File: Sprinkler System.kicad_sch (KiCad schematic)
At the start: 0 parts

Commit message: Ready to Send
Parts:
- added C1, C3: 10u, Capacitor_SMD:C_0805_2012Metric_Pad1.18x1.45mm_HandSolder, symbol Device:C_Small
- added C11, C12, C13, C14, C15, C16: 100n, Capacitor_SMD:C_0805_2012Metric_Pad1.18x1.45mm_HandSolder, symbol Device:C
- added C2: 22u, Capacitor_SMD:C_0805_2012Metric_Pad1.18x1.45mm_HandSolder, symbol Device:C_Small
- added F1: 1A, Sprinkler System:Fuseholder_5x20mm_15mm_Pins, symbol Device:Fuse
- added F2: 2A, Sprinkler System:Fuseholder_5x20mm_15mm_Pins, symbol Device:Fuse
- added J1: Main Supply, Connector_Phoenix_MC:PhoenixContact_MC_1,5_3-G-3.81_1x03_P3.81mm_Horizontal, symbol Connector:Screw_Terminal_01x03
- added J11: Station_0, Connector_Phoenix_MC:PhoenixContact_MC_1,5_2-G-3.81_1x02_P3.81mm_Horizontal, symbol Connector:Screw_Terminal_01x02
- added J12: Station_1, Connector_Phoenix_MC:PhoenixContact_MC_1,5_2-G-3.81_1x02_P3.81mm_Horizontal, symbol Connector:Screw_Terminal_01x02
- added J13: Station_2, Connector_Phoenix_MC:PhoenixContact_MC_1,5_2-G-3.81_1x02_P3.81mm_Horizontal, symbol Connector:Screw_Terminal_01x02
- added J14: Station_3, Connector_Phoenix_MC:PhoenixContact_MC_1,5_2-G-3.81_1x02_P3.81mm_Horizontal, symbol Connector:Screw_Terminal_01x02
- added J15: Station_4, Connector_Phoenix_MC:PhoenixContact_MC_1,5_2-G-3.81_1x02_P3.81mm_Horizontal, symbol Connector:Screw_Terminal_01x02
- added J16: Station_5, Connector_Phoenix_MC:PhoenixContact_MC_1,5_2-G-3.81_1x02_P3.81mm_Horizontal, symbol Connector:Screw_Terminal_01x02
- added J17: Conn_Button, Connector_JST:JST_XH_B6B-XH-A_1x06_P2.50mm_Vertical, symbol Connector_Generic:Conn_01x06
- added J2: XFMR, Connector_Phoenix_MC:PhoenixContact_MC_1,5_3-G-3.81_1x03_P3.81mm_Horizontal, symbol Connector:Screw_Terminal_01x03
- added J3: I2C, Connector_JST:JST_XH_B4B-XH-A_1x04_P2.50mm_Vertical, symbol Connector_Generic:Conn_01x04
- added J4: UART0, Connector_JST:JST_XH_B4B-XH-A_1x04_P2.50mm_Vertical, symbol Connector_Generic:Conn_01x04
- added K1: G3MB-202P, Sprinkler System:RELAY_G3MB-202P, symbol Sprinker System:G3MB-202P
- added K11, K12, K13, K14, K15, K16: G5LE-1, Relay_THT:Relay_SPDT_Omron-G5LE-1, symbol Relay:G5LE-1
- added LED1: IO2, LED_SMD:LED_0805_2012Metric_Pad1.15x1.40mm_HandSolder, symbol Device:LED_Small
- added LED2: PWR, LED_SMD:LED_0805_2012Metric_Pad1.15x1.40mm_HandSolder, symbol Device:LED_Small
- added R1, R3: 10k, Resistor_SMD:R_0805_2012Metric_Pad1.20x1.40mm_HandSolder, symbol Device:R
- added R11, R12, R13, R14, R15, R16: 100, Resistor_SMD:R_0805_2012Metric_Pad1.20x1.40mm_HandSolder, symbol Device:R
- added R2, R4: 470, Resistor_SMD:R_0805_2012Metric_Pad1.20x1.40mm_HandSolder, symbol Device:R
- added R32, R33, R34, R35: 10k, Resistor_SMD:R_0805_2012Metric_Pad1.20x1.40mm_HandSolder, symbol Device:R_Small
- added R5, R6: 4k7, Resistor_SMD:R_0805_2012Metric_Pad1.20x1.40mm_HandSolder, symbol Device:R_Small
- added RV11, RV12, RV13, RV14, RV15, RV16: 47V, Varistor:RV_Disc_D15.5mm_W5.4mm_P7.5mm, symbol Device:Varistor
- added SW1: EN, Button_Switch_SMD:SW_Push_SPST_NO_Alps_SKRK, symbol Switch:SW_Push
- added SW2: BOOT, Button_Switch_SMD:SW_Push_SPST_NO_Alps_SKRK, symbol Switch:SW_Push
- added U1: HLK-PM01, Converter_ACDC:Converter_ACDC_Hi-Link_HLK-PMxx, symbol Converter_ACDC:HLK-PM01
- added U2: ULN2803A, Package_SO:SOIC-18W_7.5x11.6mm_P1.27mm, symbol Transistor_Array:ULN2803A
- added U3: AMS1117-3.3, Package_TO_SOT_SMD:SOT-223-3_TabPin2, symbol Regulator_Linear:AMS1117-3.3
- added U4: ESP32-WROOM-32U, RF_Module:ESP32-WROOM-32U, symbol RF_Module:ESP32-WROOM-32U
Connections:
- new net: R2.1, SW1.2
- new net: C11.2, R11.1
- new net: R4.1, SW2.2
- new net: C12.2, R12.1
- new net: LED1.1 (K), R5.1
- new net: C13.2, R13.1
- new net: C14.2, R14.1
- new net: C16.2, R16.1
- new net: LED2.1 (K), R6.1
- new net: C15.2, R15.1
- new net +3V3: C2.1, C3.1, J17.2 (Pin_2), LED2.2 (A), R1.1, R3.1, U3.2 (VO), U4.2 (VDD)
- new net +5V: C1.1, J3.2 (Pin_2), J4.2 (Pin_2), K1.3, K11.5, K12.5, K13.5, K14.5, K15.5, K16.5, U1.4 (+Vout), U2.10 (COM), U3.3 (VI)
- new net 24VAC: C11.1, C12.1, C13.1, C14.1, C15.1, C16.1, F2.2, K11.1, K12.1, K13.1, K14.1, K15.1, K16.1, RV11.1, RV12.1, RV13.1, RV14.1, RV15.1, RV16.1
- new net 24VAC_Supply: F2.1, J2.3 (Pin_3)
- new net 24V_On: U2.8 (I8), U4.27 (IO16)
- new net 24V_S0: J11.2 (Pin_2), K11.3, R11.2, RV11.2
- new net 24V_S1: J12.2 (Pin_2), K12.3, R12.2, RV12.2
- new net 24V_S2: J13.2 (Pin_2), K13.3, R13.2, RV13.2
- new net 24V_S3: J14.2 (Pin_2), K14.3, R14.2, RV14.2
- new net 24V_S4: J15.2 (Pin_2), K15.3, R15.2, RV15.2
- new net 24V_S5: J16.2 (Pin_2), K16.3, R16.2, RV16.2
- new net Coil0: K11.2, U2.12 (O7)
- new net Coil1: K12.2, U2.13 (O6)
- new net Coil2: K13.2, U2.14 (O5)
- new net Coil3: K14.2, U2.15 (O4)
- new net Coil4: K15.2, U2.16 (O3)
- new net Coil5: K16.2, U2.17 (O2)
- new net EN: R1.2, SW1.1, U4.3 (EN)
- new net GND: C1.2, C2.2, C3.2, J1.1 (Pin_1), J17.1 (Pin_1), J3.1 (Pin_1), J4.1 (Pin_1), R2.2, R32.2, R33.2, R34.2, R35.2, R4.2, R5.2, R6.2, U1.3 (-Vout), U2.9 (GND), U3.1 (GND), U4.1 (GND), U4.15 (GND), U4.38 (GND), U4.39 (GND)
- new net IO0: R3.2, SW2.1, U4.25 (IO0)
- new net IO1: J4.4 (Pin_4), U4.35 (TXD0/IO1)
- new net IO2: LED1.2 (A), U4.24 (IO2)
- new net IO3: J4.3 (Pin_3), U4.34 (RXD0/IO3)
- new net IO32: J17.5 (Pin_5), R32.1, U4.8 (IO32)
- new net IO33: J17.6 (Pin_6), R33.1, U4.9 (IO33)
- new net IO34: J17.3 (Pin_3), R34.1, U4.6 (IO34)
- new net IO35: J17.4 (Pin_4), R35.1, U4.7 (IO35)
- new net L: F1.2, K1.1, U1.1 (AC/L)
- new net L_SW: J2.1 (Pin_1), K1.2
- new net L_Supply: F1.1, J1.2 (Pin_2)
- new net Neut: J1.3 (Pin_3), J11.1 (Pin_1), J12.1 (Pin_1), J13.1 (Pin_1), J14.1 (Pin_1), J15.1 (Pin_1), J16.1 (Pin_1), J2.2 (Pin_2), U1.2 (AC/N)
- new net SCL: J3.4 (Pin_4), U4.26 (IO4)
- new net SDA: J3.3 (Pin_3), U4.29 (IO5)
- new net SSR: K1.4, U2.11 (O8)
- new net Zone0: U2.7 (I7), U4.28 (IO17)
- new net Zone1: U2.6 (I6), U4.30 (IO18)
- new net Zone2: U2.5 (I5), U4.31 (IO19)
- new net Zone3: U2.4 (I4), U4.33 (IO21)
- new net Zone4: U2.3 (I3), U4.36 (IO22)
- new net Zone5: U2.2 (I2), U4.37 (IO23)
- no-connect marks 0 -> 23

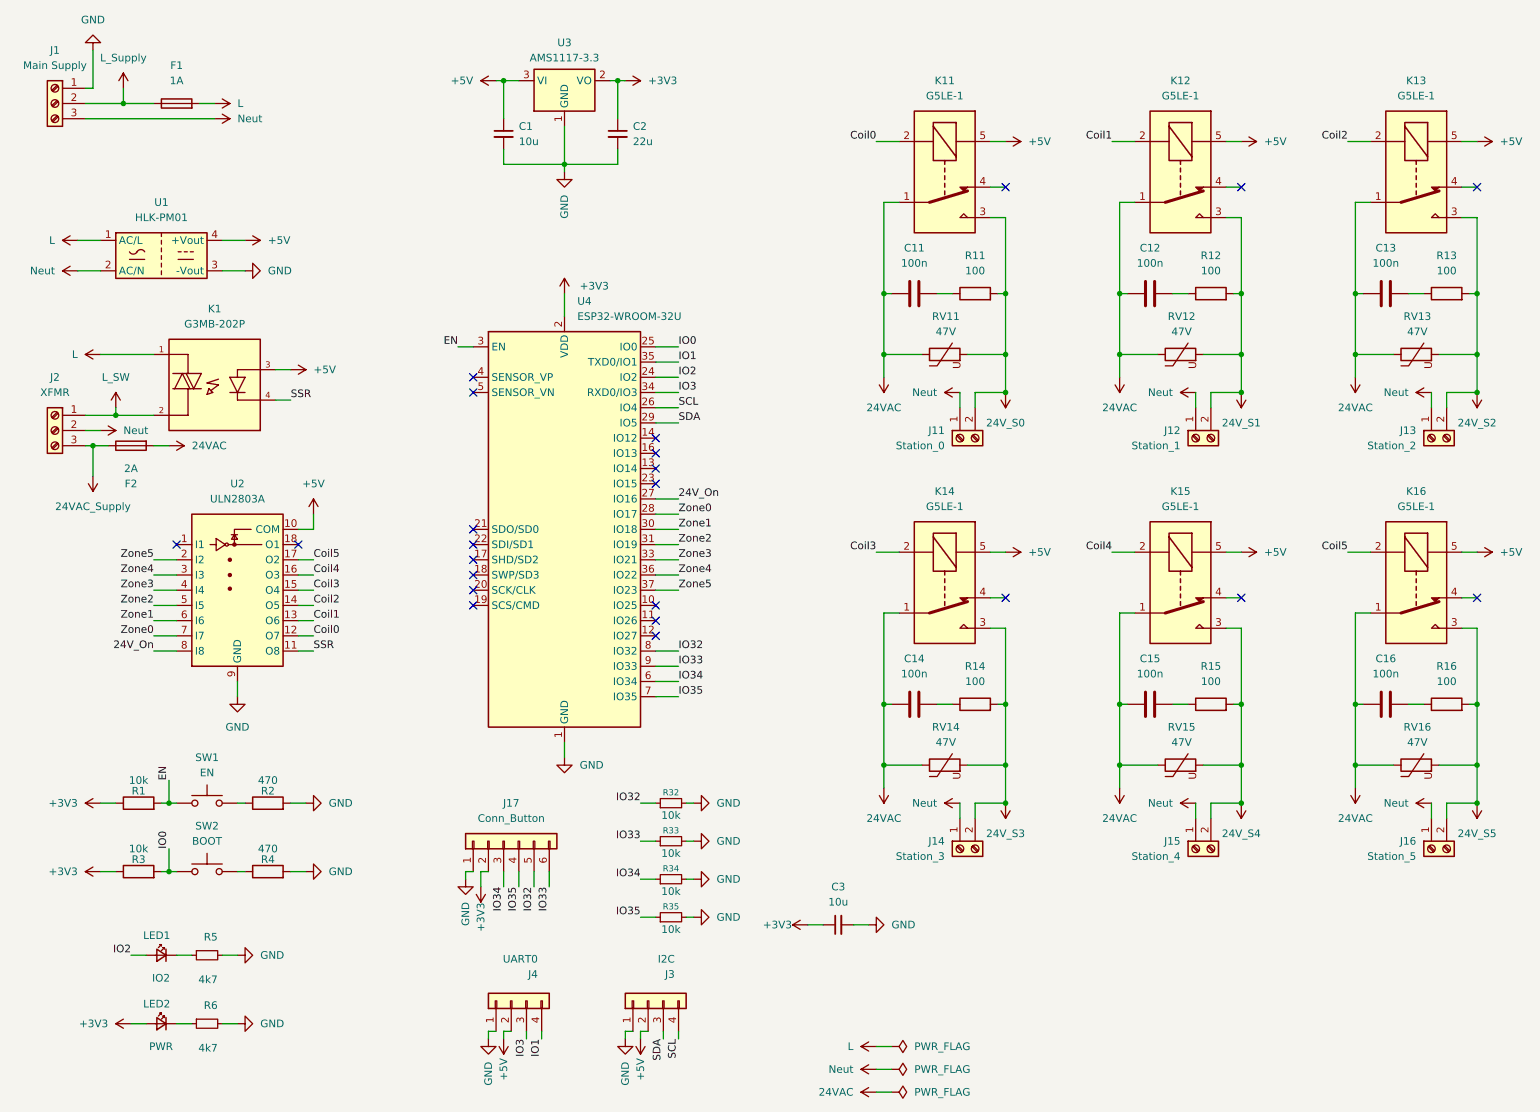
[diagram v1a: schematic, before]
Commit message: feat: advance 6-zone sprinkler controller design and documentation
* replace template docs with full project README (safety notes, enclosure guidance, power/control paths, wiring, BOM, GPIO map)
* update schematic and PCB with major reannotation/layout changes, added test points, and 24 VAC net handling refinements
* add/update project rule settings (new 24VAC net class, net class priorities, DRC exclusion updates)
* adjust relay footprint 3D model orientation/offset
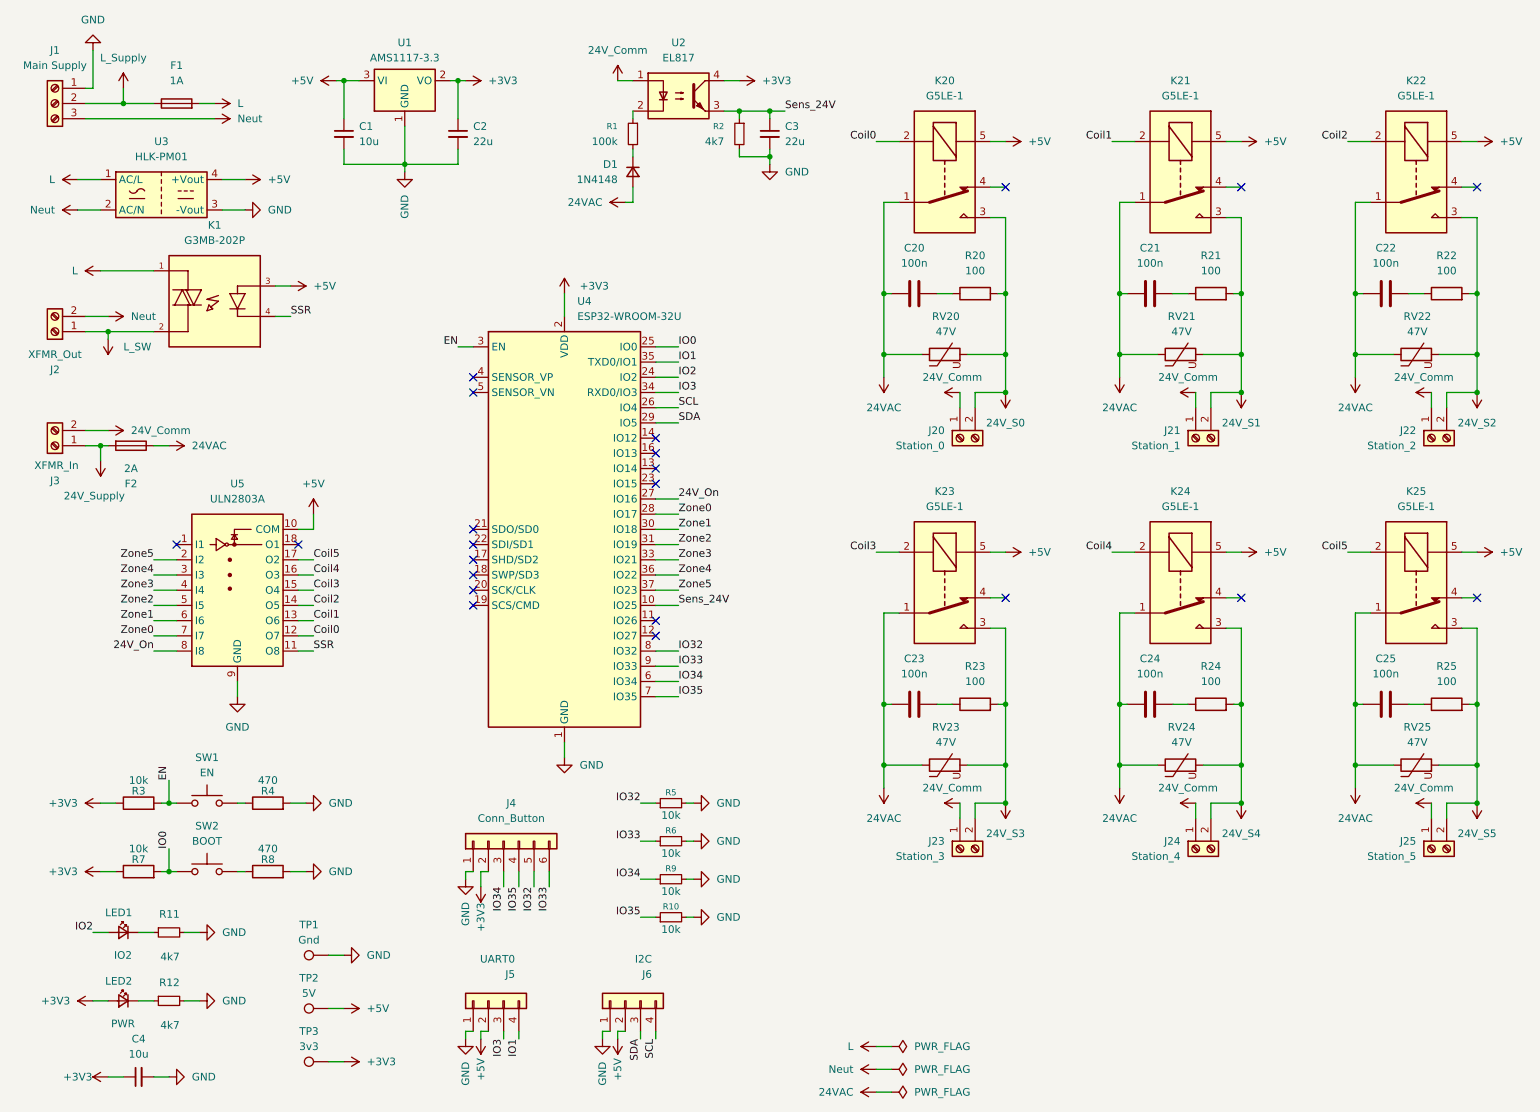
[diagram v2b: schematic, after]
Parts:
- removed J2: XFMR, Connector_Phoenix_MC:PhoenixContact_MC_1,5_3-G-3.81_1x03_P3.81mm_Horizontal, symbol Connector:Screw_Terminal_01x03
- added C3: 22u, Capacitor_SMD:C_0805_2012Metric_Pad1.18x1.45mm_HandSolder, symbol Device:C_Small
- added D1: 1N4148, Diode_SMD:D_0805_2012Metric_Pad1.15x1.40mm_HandSolder, symbol Device:D_Small
- added J2: XFMR_Out, TerminalBlock_Phoenix:TerminalBlock_Phoenix_PT-1,5-2-5.0-H_1x02_P5.00mm_Horizontal, symbol Connector:Screw_Terminal_01x02
- added J3: XFMR_In, TerminalBlock_Phoenix:TerminalBlock_Phoenix_PT-1,5-2-5.0-H_1x02_P5.00mm_Horizontal, symbol Connector:Screw_Terminal_01x02
- added R1: 100k, Resistor_SMD:R_0805_2012Metric_Pad1.20x1.40mm_HandSolder, symbol Device:R_Small
- added R2: 4k7, Resistor_SMD:R_0805_2012Metric_Pad1.20x1.40mm_HandSolder, symbol Device:R_Small
- added TP1: Gnd, TestPoint:TestPoint_Pad_D1.5mm, symbol Connector:TestPoint
- added TP2: 5V, TestPoint:TestPoint_Pad_D1.5mm, symbol Connector:TestPoint
- added TP3: 3v3, TestPoint:TestPoint_Pad_D1.5mm, symbol Connector:TestPoint
- added U2: EL817, Package_SO:SOP-4_3.8x4.1mm_P2.54mm, symbol Isolator:EL817
- renumbered C11 to C20, C12 to C21, C13 to C22, C14 to C23, C15 to C24, C16 to C25, C3 to C4, J11 to J20, J12 to J21, J13 to J22, J14 to J23, J15 to J24, J16 to J25, J17 to J4, J4 to J5, J3 to J6, K11 to K20, K12 to K21, K13 to K22, K14 to K23, K15 to K24, K16 to K25, R35 to R10, R5 to R11, R6 to R12, R11 to R20, R12 to R21, R13 to R22, R14 to R23, R15 to R24, R16 to R25, R1 to R3, R2 to R4, R32 to R5, R33 to R6, R3 to R7, R4 to R8, R34 to R9, RV11 to RV20, RV12 to RV21, RV13 to RV22, RV14 to RV23, RV15 to RV24, RV16 to RV25, U3 to U1, U1 to U3, U2 to U5
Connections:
- net 24VAC_Supply is gone; now on net 24VAC: F2.1
- net +3V3: now also TP3.1, U2.4
- net +5V: now also TP2.1
- net 24VAC: now also D1.2 (A); no longer F2.2
- net GND: now also C3.2, R2.2, TP1.1
- net L_SW: now also J2.1 (Pin_1)
- net Neut: now also J2.2 (Pin_2); no longer J20.1 (Pin_1), J21.1 (Pin_1), J22.1 (Pin_1), J23.1 (Pin_1), J24.1 (Pin_1), J25.1 (Pin_1)
- net Sens_24V: now reaches U4.10 (IO25)
- net Sens_24V: now also C3.1, R2.1, U2.3
- new net: R1.1, U2.2
- new net: D1.1 (K), R1.2
- new net 24V_Comm: J20.1 (Pin_1), J21.1 (Pin_1), J22.1 (Pin_1), J23.1 (Pin_1), J24.1 (Pin_1), J25.1 (Pin_1), J3.2 (Pin_2), U2.1
- new net 24V_Supply: F2.2, J3.1 (Pin_1)
- no-connect marks 23 -> 22
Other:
- moved on the sheet: C1, C2, C4, F2, J5, J6, K1, LED1, LED2, R11, R12, U1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

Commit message: Update PCB layout, schematic, and project config
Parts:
- added R13, R14: 4k7, Resistor_SMD:R_0805_2012Metric_Pad1.20x1.40mm_HandSolder, symbol Device:R_Small
- J1: symbol Connector:Screw_Terminal_01x03 -> Connector:Conn_01x03_Socket
- J20, J21, J22, J23, J24, J25: symbol Connector:Screw_Terminal_01x02 -> Connector:Conn_01x02_Socket
- K20, K21, K22, K23, K24, K25: value G5LE-1 -> G5LE-1-DC5
- R1: value 100k -> 10k
- RV20, RV21, RV22, RV23, RV24, RV25: value 47V -> 68V
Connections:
- net +3V3: now also R13.2, R14.2
- net SCL: now also R14.1
- net SDA: now also R13.1
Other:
- moved on the sheet: J4, J5, J6, R10, R5, R6, R9, TP1, TP2, TP3
